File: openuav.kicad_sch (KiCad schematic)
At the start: 74 parts, among them J1 Conn_01x01, J10 Conn_01x01, J11 Conn_01x01, J12 Conn_01x01, J13 Conn_01x01, J14 Conn_01x01, J15 Conn_01x01, J16 Conn_01x01, J17 Conn_01x01, J18 Conn_01x01, J19 Conn_01x01, J2 Conn_01x01, J20 Conn_01x01, J21 Conn_01x01, J22 Conn_01x01, J23 Conn_01x01, J24 Conn_01x01, J25 Conn_01x01, J26 Conn_01x01, J27 Conn_01x01, J28 Conn_01x01, J29 Conn_01x01, J3 Conn_01x01, J30 Conn_01x01, J31 Conn_01x01, J32 Conn_01x01, J33 Conn_01x01, J34 Conn_01x01, J35 Conn_01x01, J36 Conn_01x01, J37 Conn_01x01, J4 Conn_01x01, J5 Conn_01x01, J6 Conn_01x01, J7 Conn_01x01, J8 Conn_01x01, J9 Conn_01x01, J99 USB_C_Receptacle_USB2.0, U1 STM32G431CBUx, U2 BMI270, U3 BMP280, U5 TPS54202DDC, U6 W25N01GVZEIG, U7 XC6206P332MR

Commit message: Add missing JLC part numbers
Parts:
- R4: LCSC C852522 -> C25854
- U2: LCSC (none) -> C2836813
- U3: LCSC (none) -> C83291
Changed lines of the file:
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@@
       (effects (font (size 1.27 1.27)) hide)
     )
-    (property "LCSC" "C852522" (at 71.755 175.26 0)
+    (property "LCSC" "C25854" (at 71.755 175.26 0)
       (effects (font (size 1.27 1.27)) hide)
     )
@@
     )
     (property "Datasheet" "https://www.bosch-sensortec.com/media/boschsensortec/downloads/datasheets/bst-bmi160-ds000.pdf" (at 114.3 29.21 0)
+      (effects (font (size 1.27 1.27)) hide)
+    )
+    (property "LCSC" "C2836813" (at 132.08 50.8 0)
       (effects (font (size 1.27 1.27)) hide)
     )
@@
       (effects (font (size 1.27 1.27)) hide)
     )
+    (property "LCSC" "C83291" (at 187.96 50.8 0)
+      (effects (font (size 1.27 1.27)) hide)
+    )

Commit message: fix JLC 10k resistor part numbers
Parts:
- R6, R8: LCSC C17414 -> C25744
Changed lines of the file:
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@@
       (effects (font (size 1.27 1.27)) hide)
     )
-    (property "LCSC" "C17414" (at 269.494 172.72 0)
+    (property "LCSC" "C25744" (at 269.494 172.72 0)
       (effects (font (size 1.27 1.27)) hide)
     )
@@
       (effects (font (size 1.27 1.27)) hide)
     )
-    (property "LCSC" "C17414" (at 78.74 139.7 0)
+    (property "LCSC" "C25744" (at 78.74 139.7 0)
       (effects (font (size 1.27 1.27)) hide)
     )

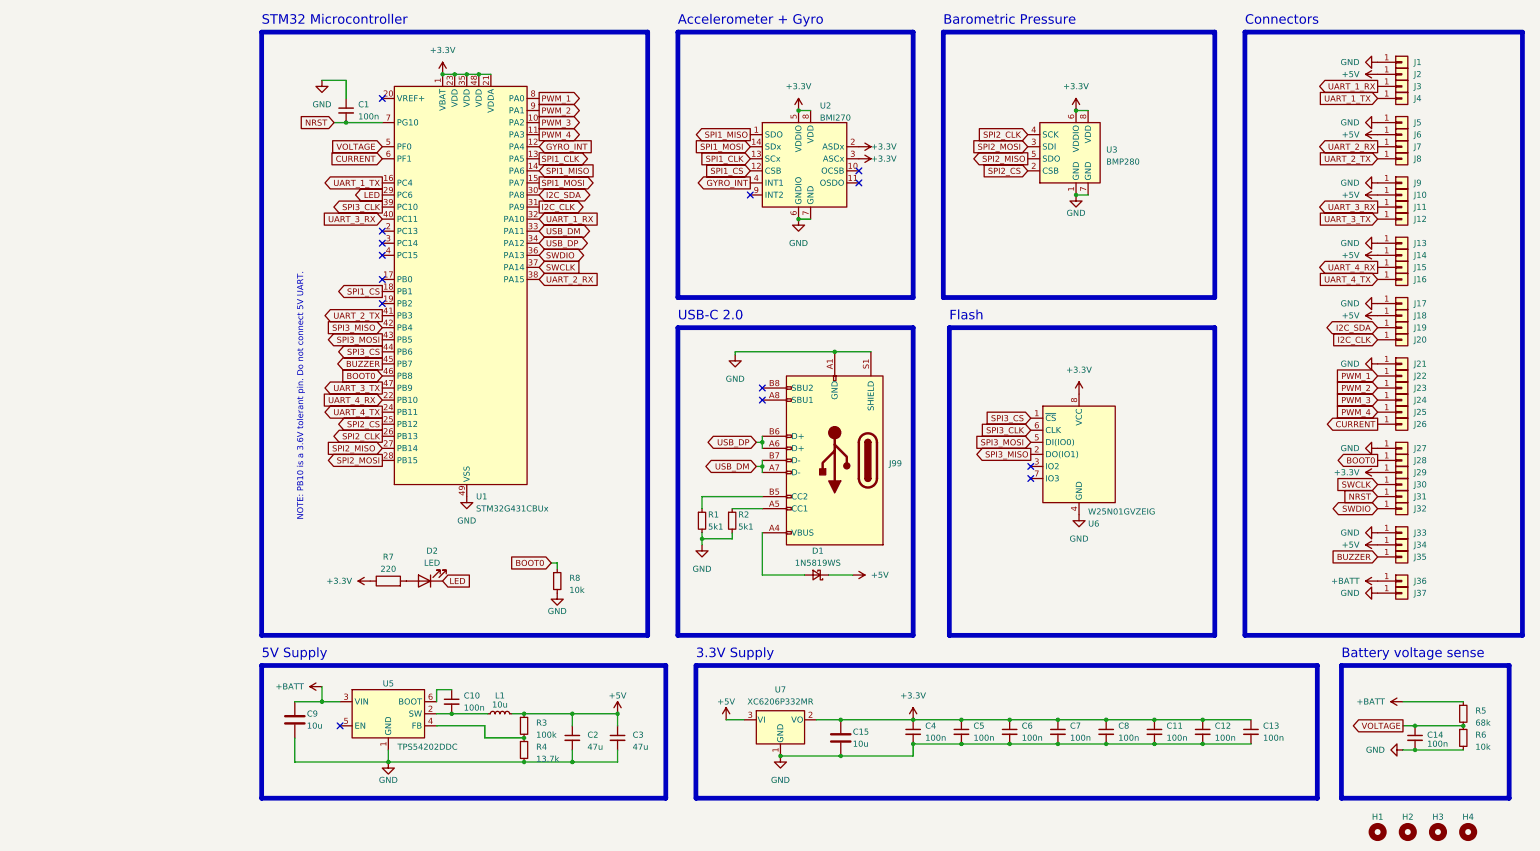
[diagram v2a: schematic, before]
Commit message: begin work on STM32G474 version
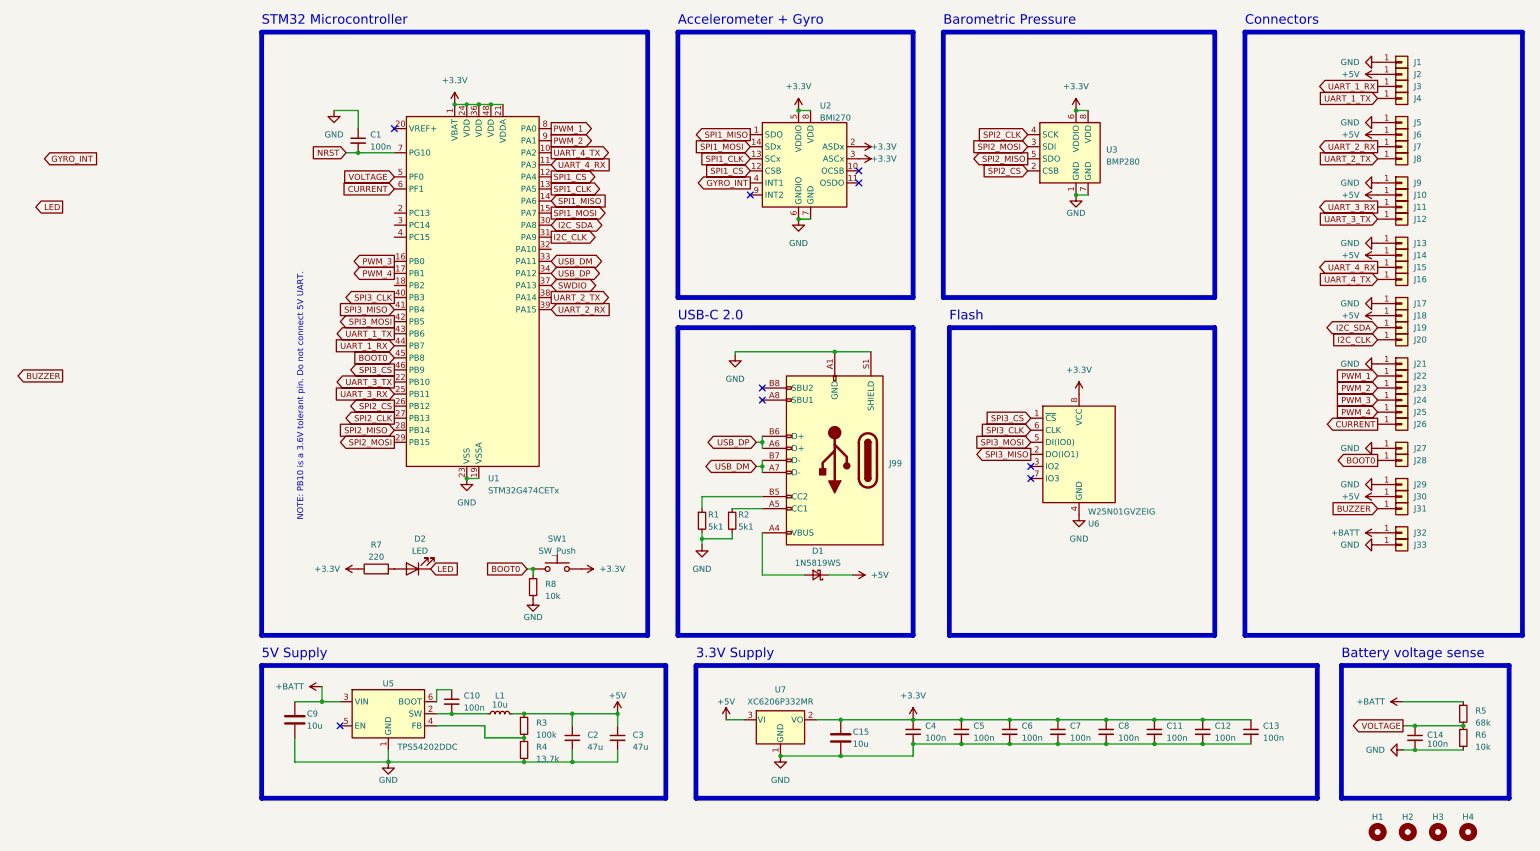
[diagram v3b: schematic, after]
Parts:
- removed J34, J35, J36, J37: Conn_01x01, Connector_Custom_Pads:TP-2.54, symbol Connector_Generic:Conn_01x01
- removed U1: STM32G431CBUx, Package_DFN_QFN:QFN-48-1EP_7x7mm_P0.5mm_EP5.6x5.6mm, symbol MCU_ST_STM32G4:STM32G431CBUx
- added SW1: SW_Push, symbol Switch:SW_Push
- added U1: STM32G474CETx, Package_QFP:LQFP-48_7x7mm_P0.5mm, symbol MCU_ST_STM32G4:STM32G474CETx
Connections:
- net SWCLK is gone; now on net +5V: J30.1 (Pin_1)
- net +3V3: now also SW1.2, U1.1 (VBAT), U1.21 (VDDA), U1.24 (VDD), U1.36 (VDD), U1.48 (VDD); no longer J29.1 (Pin_1)
- net +BATT: now also J32.1 (Pin_1)
- net BOOT0: now also SW1.1, U1.45 (PB8)
- net BUZZER: now also J31.1 (Pin_1)
- net CURRENT: now also U1.6 (PF1)
- net GND: now also J29.1 (Pin_1), U1.19 (VSSA), U1.23 (VSS), U1.35 (VSS), U1.47 (VSS)
- net I2C_CLK: now also U1.31 (PA9)
- net I2C_SDA: now also U1.30 (PA8)
- net NRST: now also U1.7 (PG10); no longer J31.1 (Pin_1)
- net PWM_1: now also U1.8 (PA0)
- net PWM_2: now also U1.9 (PA1)
- net PWM_3: now also U1.16 (PB0)
- net PWM_4: now also U1.17 (PB1)
- net SPI1_CLK: now also U1.13 (PA5)
- net SPI1_CS: now also U1.12 (PA4)
- net SPI1_MISO: now also U1.14 (PA6)
- net SPI1_MOSI: now also U1.15 (PA7)
- net SPI2_CLK: now also U1.27 (PB13)
- net SPI2_CS: now also U1.26 (PB12)
- net SPI2_MISO: now also U1.28 (PB14)
- net SPI2_MOSI: now also U1.29 (PB15)
- net SPI3_CLK: now also U1.40 (PB3)
- net SPI3_CS: now also U1.46 (PB9)
- net SPI3_MISO: now also U1.41 (PB4)
- net SPI3_MOSI: now also U1.42 (PB5)
- net SWDIO: now also U1.37 (PA13); no longer J32.1 (Pin_1)
- net UART_1_RX: now also U1.44 (PB7)
- net UART_1_TX: now also U1.43 (PB6)
- net UART_2_RX: now also U1.39 (PA15)
- net UART_2_TX: now also U1.38 (PA14)
- net UART_3_RX: now also U1.25 (PB11)
- net UART_3_TX: now also U1.22 (PB10)
- net UART_4_RX: now also U1.11 (PA3)
- net UART_4_TX: now also U1.10 (PA2)
- net USB_DM: now also U1.33 (PA11)
- net USB_DP: now also U1.34 (PA12)
- net VOLTAGE: now also U1.5 (PF0)
- no-connect marks 14 -> 9
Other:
- moved on the sheet: C1, D2, J29, J30, J31, J32, J33, R7, R8

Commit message: continue g474 redesign
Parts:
- removed J32, J33: Conn_01x01, Connector_Custom_Pads:TP-2.54, symbol Connector_Generic:Conn_01x01
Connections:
- net +5V: now also J28.1 (Pin_1); no longer J30.1 (Pin_1)
- net +BATT: now also J30.1 (Pin_1)
- net BOOT0: no longer J28.1 (Pin_1)
- net BUZZER: now also J29.1 (Pin_1), U1.2 (PC13); no longer J31.1 (Pin_1)
- net GND: now also J31.1 (Pin_1); no longer J29.1 (Pin_1)
- net GYRO_INT: now also U1.18 (PB2)
- net LED: now also U1.32 (PA10)
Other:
- moved on the sheet: J29

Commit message: continued work on G474 board
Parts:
- added C16: 100n, Capacitor_SMD:C_0402_1005Metric, symbol Device:C_Small
- L1: footprint Inductor_SMD:L_Sunlord_MWSA0603S -> Inductor_SMD:L_Sunlord_MWSA0402S; LCSC C132141 -> C408339
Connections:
- net +3V3: now also C16.1
- net GND: now also C16.2
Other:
- moved on the sheet: U6
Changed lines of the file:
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@@
   (junction (at 59.69 39.37) (diameter 0) (color 0 0 0 0)
   )
+  (junction (at 224.79 168.91) (diameter 0) (color 0 0 0 0)
+  )
   (junction (at 121.92 115.57) (diameter 0) (color 0 0 0 0)
   )
@@
   (junction (at 214.63 173.99) (diameter 0) (color 0 0 0 0)
   )
+  (junction (at 224.79 173.99) (diameter 0) (color 0 0 0 0)
+  )
   (junction (at 71.755 172.72) (diameter 0) (color 0 0 0 0)
   )
@@
   (no_connect (at 44.45 44.45))
   (no_connect (at 142.24 55.88))
-  (no_connect (at 178.435 118.11))
+  (no_connect (at 179.07 118.11))
   (no_connect (at 121.92 99.06))
   (no_connect (at 142.24 53.34))
   (no_connect (at 121.92 101.6))
   (no_connect (at 119.38 58.42))
-  (no_connect (at 178.435 115.57))
+  (no_connect (at 179.07 115.57))
   (no_connect (at 33.02 170.18))
   (wire (pts (xy 36.83 49.53) (xy 44.45 49.53))
@@
     (stroke (width 0) (type default))
   )
+  (wire (pts (xy 224.79 173.99) (xy 234.95 173.99))
+    (stroke (width 0) (type default))
+  )
   (wire (pts (xy 63.5 170.18) (xy 63.5 172.72))
     (stroke (width 0) (type default))
@@
     (stroke (width 0) (type default))
   )
+  (wire (pts (xy 224.79 168.91) (xy 234.95 168.91))
+    (stroke (width 0) (type default))
+  )
   (wire (pts (xy 81.915 177.8) (xy 91.44 177.8))
     (stroke (width 0) (type default))
@@
     )
   )
-  (global_label "SPI3_CS" (shape input) (at 178.435 105.41 180) (fields_autoplaced)
+  (global_label "SPI3_CS" (shape input) (at 179.07 105.41 180) (fields_autoplaced)
     (effects (font (size 1.27 1.27)) (justify right))
-    (property "Intersheetrefs" "${INTERSHEET_REFS}" (at 167.7883 105.41 0)
+    (property "Intersheetrefs" "${INTERSHEET_REFS}" (at 168.4233 105.41 0)
       (effects (font (size 1.27 1.27)) (justify right) hide)
     )
@@
     )
   )
-  (global_label "SPI3_MOSI" (shape input) (at 178.435 110.49 180) (fields_autoplaced)
+  (global_label "SPI3_MOSI" (shape input) (at 179.07 110.49 180) (fields_autoplaced)
     (effects (font (size 1.27 1.27)) (justify right))
-    (property "Intersheetrefs" "${INTERSHEET_REFS}" (at 165.6716 110.49 0)
+    (property "Intersheetrefs" "${INTERSHEET_REFS}" (at 166.3066 110.49 0)
       (effects (font (size 1.27 1.27)) (justify right) hide)
     )
@@
     )
   )
-  (global_label "SPI3_MISO" (shape output) (at 178.435 113.03 180) (fields_autoplaced)
+  (global_label "SPI3_MISO" (shape output) (at 179.07 113.03 180) (fields_autoplaced)
     (effects (font (size 1.27 1.27)) (justify right))
-    (property "Intersheetrefs" "${INTERSHEET_REFS}" (at 165.6716 113.03 0)
+    (property "Intersheetrefs" "${INTERSHEET_REFS}" (at 166.3066 113.03 0)
       (effects (font (size 1.27 1.27)) (justify right) hide)
     )
@@
     )
   )
-  (global_label "SPI3_CLK" (shape input) (at 178.435 107.95 180) (fields_autoplaced)
+  (global_label "SPI3_CLK" (shape input) (at 179.07 107.95 180) (fields_autoplaced)
     (effects (font (size 1.27 1.27)) (justify right))
-    (property "Intersheetrefs" "${INTERSHEET_REFS}" (at 166.6997 107.95 0)
+    (property "Intersheetrefs" "${INTERSHEET_REFS}" (at 167.3347 107.95 0)
       (effects (font (size 1.27 1.27)) (justify right) hide)
     )
@@
     )
   )
-  (symbol (lib_id "Memory_Flash:W25Q32JVSS") (at 188.595 113.03 0) (unit 1)
+  (symbol (lib_id "Memory_Flash:W25Q32JVSS") (at 189.23 113.03 0) (unit 1)
     (in_bom yes) (on_board yes) (dnp no)
-    (property "Reference" "U6" (at 190.5 127.635 0)
+    (property "Reference" "U6" (at 191.135 127.635 0)
       (effects (font (size 1.27 1.27)) (justify left))
     )
-    (property "Value" "W25N01GVZEIG" (at 190.5 125.095 0)
+    (property "Value" "W25N01GVZEIG" (at 191.135 125.095 0)
       (effects (font (size 1.27 1.27)) (justify left))
     )
-    (property "Footprint" "Package_SON:WSON-8-1EP_8x6mm_P1.27mm_EP3.4x4.3mm" (at 188.595 113.03 0)
+    (property "Footprint" "Package_SON:WSON-8-1EP_8x6mm_P1.27mm_EP3.4x4.3mm" (at 189.23 113.03 0)
       (effects (font (size 1.27 1.27)) hide)
     )
-    (property "Datasheet" "http://www.winbond.com/resource-files/w25q32jv%20revg%2003272018%20plus.pdf" (at 188.595 113.03 0)
+    (property "Datasheet" "http://www.winbond.com/resource-files/w25q32jv%20revg%2003272018%20plus.pdf" (at 189.23 113.03 0)
       (effects (font (size 1.27 1.27)) hide)
     )
-    (property "LCSC" "C88868" (at 188.595 113.03 0)
+    (property "LCSC" "C88868" (at 189.23 113.03 0)
       (effects (font (size 1.27 1.27)) hide)
     )
@@
       (effects (font (size 1.27 1.27)))
     )
-    (property "Footprint" "Inductor_SMD:L_Sunlord_MWSA0603S" (at 66.675 167.64 0)
+    (property "Footprint" "Inductor_SMD:L_Sunlord_MWSA0402S" (at 66.675 167.64 0)
       (effects (font (size 1.27 1.27)) hide)
     )
@@
       (effects (font (size 1.27 1.27)) hide)
     )
-    (property "LCSC" "C132141" (at 66.675 167.64 0)
+    (property "LCSC" "C408339" (at 66.675 167.64 0)
       (effects (font (size 1.27 1.27)) hide)
     )
@@
     )
   )
-  (symbol (lib_id "power:+3.3V") (at 188.595 100.33 0) (unit 1)
+  (symbol (lib_id "power:+3.3V") (at 189.23 100.33 0) (unit 1)
     (in_bom yes) (on_board yes) (dnp no) (fields_autoplaced)
-    (property "Reference" "#PWR01" (at 188.595 104.14 0)
+    (property "Reference" "#PWR01" (at 189.23 104.14 0)
       (effects (font (size 1.27 1.27)) hide)
     )
-    (property "Value" "+3.3V" (at 188.595 95.25 0)
+    (property "Value" "+3.3V" (at 189.23 95.25 0)
       (effects (font (size 1.27 1.27)))
     )
-    (property "Footprint" "" (at 188.595 100.33 0)
+    (property "Footprint" "" (at 189.23 100.33 0)
       (effects (font (size 1.27 1.27)) hide)
     )
-    (property "Datasheet" "" (at 188.595 100.33 0)
+    (property "Datasheet" "" (at 189.23 100.33 0)
       (effects (font (size 1.27 1.27)) hide)
     )
@@
     )
   )
-  (symbol (lib_id "power:GND") (at 188.595 125.73 0) (unit 1)
+  (symbol (lib_id "power:GND") (at 189.23 125.73 0) (unit 1)
     (in_bom yes) (on_board yes) (dnp no) (fields_autoplaced)
-    (property "Reference" "#PWR03" (at 188.595 132.08 0)
+    (property "Reference" "#PWR03" (at 189.23 132.08 0)
       (effects (font (size 1.27 1.27)) hide)
     )
-    (property "Value" "GND" (at 188.595 130.81 0)
+    (property "Value" "GND" (at 189.23 130.81 0)
       (effects (font (size 1.27 1.27)))
     )
-    (property "Footprint" "" (at 188.595 125.73 0)
+    (property "Footprint" "" (at 189.23 125.73 0)
       (effects (font (size 1.27 1.27)) hide)
     )
-    (property "Datasheet" "" (at 188.595 125.73 0)
+    (property "Datasheet" "" (at 189.23 125.73 0)
       (effects (font (size 1.27 1.27)) hide)
     )
@@
         )
       )
+    )
+  )
+  (symbol (lib_id "Device:C_Small") (at 234.95 171.45 0) (unit 1)
+    (in_bom yes) (on_board yes) (dnp no) (fields_autoplaced)
+    (property "Reference" "C16" (at 237.49 170.1862 0)
+      (effects (font (size 1.27 1.27)) (justify left))
+    )
+    (property "Value" "100n" (at 237.49 172.7262 0)
+      (effects (font (size 1.27 1.27)) (justify left))
+    )
+    (property "Footprint" "Capacitor_SMD:C_0402_1005Metric" (at 234.95 171.45 0)
+      (effects (font (size 1.27 1.27)) hide)
+    )
+    (property "Datasheet" "~" (at 234.95 171.45 0)
+      (effects (font (size 1.27 1.27)) hide)
+    )
+    (property "LCSC" "C307331" (at 234.95 171.45 0)
+      (effects (font (size 1.27 1.27)) hide)
+    )
+    (pin "1")
+    (pin "2")
+    (instances
+      (project "openuav"
+        (path "/e63e39d7-6ac0-4ffd-8aa3-1841a4541b55"
+          (reference "C16") (unit 1)
+        )
+      )

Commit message: routing
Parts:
- removed C3: 47u, Capacitor_SMD:C_1206_3216Metric, symbol Device:C_Small
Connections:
- net CURRENT: now also U1.5 (PF0); no longer U1.6 (PF1)
- net VOLTAGE: now also U1.6 (PF1); no longer U1.5 (PF0)
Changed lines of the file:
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@@
   (junction (at 121.92 115.57) (diameter 0) (color 0 0 0 0)
   )
-  (junction (at 81.915 177.8) (diameter 0) (color 0 0 0 0)
-  )
   (junction (at 138.43 168.91) (diameter 0) (color 0 0 0 0)
   )
@@
   (junction (at 224.79 173.99) (diameter 0) (color 0 0 0 0)
   )
+  (junction (at 81.28 167.64) (diameter 0) (color 0 0 0 0)
+  )
   (junction (at 71.755 172.72) (diameter 0) (color 0 0 0 0)
   )
@@
   (junction (at 184.15 168.91) (diameter 0) (color 0 0 0 0)
   )
-  (junction (at 81.915 167.64) (diameter 0) (color 0 0 0 0)
-  )
   (junction (at 194.31 168.91) (diameter 0) (color 0 0 0 0)
   )
@@
   )
   (junction (at 57.15 39.37) (diameter 0) (color 0 0 0 0)
-  )
-  (junction (at 91.44 167.64) (diameter 0) (color 0 0 0 0)
   )
   (junction (at 59.69 118.11) (diameter 0) (color 0 0 0 0)
@@
     (stroke (width 0) (type default))
   )
+  (wire (pts (xy 81.28 167.64) (xy 81.915 167.64))
+    (stroke (width 0) (type default))
+  )
   (wire (pts (xy 109.22 121.92) (xy 109.22 124.46))
     (stroke (width 0) (type default))
@@
     (stroke (width 0) (type default))
   )
-  (wire (pts (xy 81.915 167.64) (xy 91.44 167.64))
-    (stroke (width 0) (type default))
-  )
   (wire (pts (xy 64.77 39.37) (xy 67.31 39.37))
     (stroke (width 0) (type default))
@@
     (stroke (width 0) (type default))
   )
-  (wire (pts (xy 71.755 167.64) (xy 81.915 167.64))
-    (stroke (width 0) (type default))
-  )
-  (wire (pts (xy 91.44 175.26) (xy 91.44 177.8))
+  (wire (pts (xy 71.755 167.64) (xy 81.28 167.64))
     (stroke (width 0) (type default))
   )
@@
     (stroke (width 0) (type default))
   )
-  (wire (pts (xy 91.44 167.64) (xy 91.44 170.18))
-    (stroke (width 0) (type default))
-  )
   (wire (pts (xy 184.15 173.99) (xy 194.31 173.99))
     (stroke (width 0) (type default))
@@
   )
   (wire (pts (xy 224.79 168.91) (xy 234.95 168.91))
-    (stroke (width 0) (type default))
-  )
-  (wire (pts (xy 81.915 177.8) (xy 91.44 177.8))
     (stroke (width 0) (type default))
   )
@@
     )
   )
-  (global_label "CURRENT" (shape input) (at 44.45 57.15 180) (fields_autoplaced)
-    (effects (font (size 1.27 1.27)) (justify right))
-    (property "Intersheetrefs" "${INTERSHEET_REFS}" (at 32.9566 57.15 0)
+  (global_label "CURRENT" (shape input) (at 44.45 54.61 180) (fields_autoplaced)
+    (effects (font (size 1.27 1.27)) (justify right))
+    (property "Intersheetrefs" "${INTERSHEET_REFS}" (at 32.9566 54.61 0)
       (effects (font (size 1.27 1.27)) (justify right) hide)
     )
@@
     )
   )
-  (global_label "VOLTAGE" (shape input) (at 44.45 54.61 180) (fields_autoplaced)
-    (effects (font (size 1.27 1.27)) (justify right))
-    (property "Intersheetrefs" "${INTERSHEET_REFS}" (at 33.6218 54.61 0)
+  (global_label "VOLTAGE" (shape input) (at 44.45 57.15 180) (fields_autoplaced)
+    (effects (font (size 1.27 1.27)) (justify right))
+    (property "Intersheetrefs" "${INTERSHEET_REFS}" (at 33.6218 57.15 0)
       (effects (font (size 1.27 1.27)) (justify right) hide)
     )
@@
     )
   )
-  (symbol (lib_id "power:+5V") (at 91.44 167.64 0) (unit 1)
+  (symbol (lib_id "power:+5V") (at 81.28 167.64 0) (unit 1)
     (in_bom yes) (on_board yes) (dnp no) (fields_autoplaced)
-    (property "Reference" "#PWR07" (at 91.44 171.45 0)
-      (effects (font (size 1.27 1.27)) hide)
-    )
-    (property "Value" "+5V" (at 91.44 163.83 0)
+    (property "Reference" "#PWR07" (at 81.28 171.45 0)
+      (effects (font (size 1.27 1.27)) hide)
+    )
+    (property "Value" "+5V" (at 81.28 163.83 0)
       (effects (font (size 1.27 1.27)))
     )
-    (property "Footprint" "" (at 91.44 167.64 0)
-      (effects (font (size 1.27 1.27)) hide)
-    )
-    (property "Datasheet" "" (at 91.44 167.64 0)
+    (property "Footprint" "" (at 81.28 167.64 0)
+      (effects (font (size 1.27 1.27)) hide)
+    )
+    (property "Datasheet" "" (at 81.28 167.64 0)
       (effects (font (size 1.27 1.27)) hide)
     )
@@
         )
       )
-    )
-  )
-  (symbol (lib_id "Device:C_Small") (at 91.44 172.72 0) (unit 1)
-    (in_bom yes) (on_board yes) (dnp no) (fields_autoplaced)
-    (property "Reference" "C3" (at 94.615 172.0913 0)
-      (effects (font (size 1.27 1.27)) (justify left))
-    )
-    (property "Value" "47u" (at 94.615 174.6313 0)
-      (effects (font (size 1.27 1.27)) (justify left))
-    )
-    (property "Footprint" "Capacitor_SMD:C_1206_3216Metric" (at 91.44 172.72 0)
-      (effects (font (size 1.27 1.27)) hide)
-    )
-    (property "Datasheet" "~" (at 91.44 172.72 0)
-      (effects (font (size 1.27 1.27)) hide)
-    )
-    (property "LCSC" "C96123" (at 91.44 172.72 0)
-      (effects (font (size 1.27 1.27)) hide)
-    )
-    (pin "1")
-    (pin "2")
-    (instances
-      (project "openuav"
-        (path "/e63e39d7-6ac0-4ffd-8aa3-1841a4541b55"
-          (reference "C3") (unit 1)
-        )
-      )
